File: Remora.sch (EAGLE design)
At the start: 81 parts, among them IC1 MCP23017, J2 GROVE-I2C, P1 PADSMALL, T1 2N3904, T2 BSS138

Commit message: Mise à jour du PCB et ajout d'images
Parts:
- RELAIS: value G3MC-202P -> G3MC-202P-5V
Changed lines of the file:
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@@
 <grid distance="0.1" unitdist="inch" unit="inch" style="lines" multiple="1" display="no" altdistance="0.01" altunitdist="inch" altunit="inch"/>
 <layers>
-<layer number="1" name="Top" color="4" fill="1" visible="no" active="no"/>
-<layer number="2" name="Route2" color="1" fill="3" visible="no" active="no"/>
-<layer number="3" name="Route3" color="4" fill="3" visible="no" active="no"/>
-<layer number="4" name="Route4" color="1" fill="4" visible="no" active="no"/>
-<layer number="5" name="Route5" color="4" fill="4" visible="no" active="no"/>
-<layer number="6" name="Route6" color="1" fill="8" visible="no" active="no"/>
-<layer number="7" name="Route7" color="4" fill="8" visible="no" active="no"/>
-<layer number="8" name="Route8" color="1" fill="2" visible="no" active="no"/>
-<layer number="9" name="Route9" color="4" fill="2" visible="no" active="no"/>
-<layer number="10" name="Route10" color="1" fill="7" visible="no" active="no"/>
-<layer number="11" name="Route11" color="4" fill="7" visible="no" active="no"/>
-<layer number="12" name="Route12" color="1" fill="5" visible="no" active="no"/>
-<layer number="13" name="Route13" color="4" fill="5" visible="no" active="no"/>
-<layer number="14" name="Route14" color="1" fill="6" visible="no" active="no"/>
-<layer number="15" name="Route15" color="4" fill="6" visible="no" active="no"/>
-<layer number="16" name="Bottom" color="1" fill="1" visible="no" active="no"/>
-<layer number="17" name="Pads" color="2" fill="1" visible="no" active="no"/>
-<layer number="18" name="Vias" color="2" fill="1" visible="no" active="no"/>
-<layer number="19" name="Unrouted" color="13" fill="1" visible="no" active="no"/>
-<layer number="20" name="Dimension" color="15" fill="1" visible="no" active="no"/>
-<layer number="21" name="tPlace" color="7" fill="1" visible="no" active="no"/>
-<layer number="22" name="bPlace" color="3" fill="1" visible="no" active="no"/>
-<layer number="23" name="tOrigins" color="15" fill="1" visible="no" active="no"/>
-<layer number="24" name="bOrigins" color="3" fill="1" visible="no" active="no"/>
-<layer number="25" name="tNames" color="7" fill="1" visible="no" active="no"/>
-<layer number="26" name="bNames" color="3" fill="1" visible="no" active="no"/>
-<layer number="27" name="tValues" color="7" fill="1" visible="no" active="no"/>
-<layer number="28" name="bValues" color="3" fill="1" visible="no" active="no"/>
+<layer number="1" name="Top" color="4" fill="1" visible="yes" active="no"/>
+<layer number="2" name="Route2" color="1" fill="3" visible="yes" active="no"/>
+<layer number="3" name="Route3" color="4" fill="3" visible="yes" active="no"/>
+<layer number="4" name="Route4" color="1" fill="4" visible="yes" active="no"/>
+<layer number="5" name="Route5" color="4" fill="4" visible="yes" active="no"/>
+<layer number="6" name="Route6" color="1" fill="8" visible="yes" active="no"/>
+<layer number="7" name="Route7" color="4" fill="8" visible="yes" active="no"/>
+<layer number="8" name="Route8" color="1" fill="2" visible="yes" active="no"/>
+<layer number="9" name="Route9" color="4" fill="2" visible="yes" active="no"/>
+<layer number="10" name="Route10" color="1" fill="7" visible="yes" active="no"/>
+<layer number="11" name="Route11" color="4" fill="7" visible="yes" active="no"/>
+<layer number="12" name="Route12" color="1" fill="5" visible="yes" active="no"/>
+<layer number="13" name="Route13" color="4" fill="5" visible="yes" active="no"/>
+<layer number="14" name="Route14" color="1" fill="6" visible="yes" active="no"/>
+<layer number="15" name="Route15" color="4" fill="6" visible="yes" active="no"/>
+<layer number="16" name="Bottom" color="1" fill="1" visible="yes" active="no"/>
+<layer number="17" name="Pads" color="2" fill="1" visible="yes" active="no"/>
+<layer number="18" name="Vias" color="2" fill="1" visible="yes" active="no"/>
+<layer number="19" name="Unrouted" color="13" fill="1" visible="yes" active="no"/>
+<layer number="20" name="Dimension" color="15" fill="1" visible="yes" active="no"/>
+<layer number="21" name="tPlace" color="7" fill="1" visible="yes" active="no"/>
+<layer number="22" name="bPlace" color="3" fill="1" visible="yes" active="no"/>
+<layer number="23" name="tOrigins" color="15" fill="1" visible="yes" active="no"/>
+<layer number="24" name="bOrigins" color="3" fill="1" visible="yes" active="no"/>
+<layer number="25" name="tNames" color="7" fill="1" visible="yes" active="no"/>
+<layer number="26" name="bNames" color="3" fill="1" visible="yes" active="no"/>
+<layer number="27" name="tValues" color="7" fill="1" visible="yes" active="no"/>
+<layer number="28" name="bValues" color="3" fill="1" visible="yes" active="no"/>
 <layer number="29" name="tStop" color="7" fill="3" visible="no" active="no"/>
 <layer number="30" name="bStop" color="7" fill="6" visible="no" active="no"/>
@@
 <layer number="35" name="tGlue" color="7" fill="4" visible="no" active="no"/>
 <layer number="36" name="bGlue" color="7" fill="5" visible="no" active="no"/>
-<layer number="37" name="tTest" color="7" fill="1" visible="no" active="no"/>
-<layer number="38" name="bTest" color="7" fill="1" visible="no" active="no"/>
+<layer number="37" name="tTest" color="7" fill="1" visible="yes" active="no"/>
+<layer number="38" name="bTest" color="7" fill="1" visible="yes" active="no"/>
 <layer number="39" name="tKeepout" color="4" fill="11" visible="no" active="no"/>
 <layer number="40" name="bKeepout" color="1" fill="11" visible="no" active="no"/>
@@
 <layer number="44" name="Drills" color="7" fill="1" visible="no" active="no"/>
 <layer number="45" name="Holes" color="7" fill="1" visible="no" active="no"/>
-<layer number="46" name="Milling" color="3" fill="1" visible="no" active="no"/>
-<layer number="47" name="Measures" color="7" fill="1" visible="no" active="no"/>
-<layer number="48" name="Document" color="7" fill="1" visible="no" active="no"/>
-<layer number="49" name="Reference" color="7" fill="1" visible="no" active="no"/>
-<layer number="50" name="dxf" color="7" fill="1" visible="no" active="no"/>
-<layer number="51" name="tDocu" color="7" fill="1" visible="no" active="no"/>
-<layer number="52" name="bDocu" color="3" fill="1" visible="no" active="no"/>
-<layer number="53" name="tGND_GNDA" color="7" fill="9" visible="no" active="no"/>
-<layer number="54" name="bGND_GNDA" color="1" fill="9" visible="no" active="no"/>
-<layer number="56" name="wert" color="7" fill="1" visible="no" active="no"/>
-<layer number="57" name="tCAD" color="7" fill="1" visible="no" active="no"/>
-<layer number="59" name="tCarbon" color="7" fill="1" visible="no" active="no"/>
-<layer number="60" name="bCarbon" color="7" fill="1" visible="no" active="no"/>
+<layer number="46" name="Milling" color="3" fill="1" visible="yes" active="no"/>
+<layer number="47" name="Measures" color="7" fill="1" visible="yes" active="no"/>
+<layer number="48" name="Document" color="7" fill="1" visible="yes" active="no"/>
+<layer number="49" name="Reference" color="7" fill="1" visible="yes" active="no"/>
+<layer number="50" name="dxf" color="7" fill="1" visible="yes" active="no"/>
+<layer number="51" name="tDocu" color="7" fill="1" visible="yes" active="no"/>
+<layer number="52" name="bDocu" color="3" fill="1" visible="yes" active="no"/>
+<layer number="53" name="tGND_GNDA" color="7" fill="9" visible="yes" active="no"/>
+<layer number="54" name="bGND_GNDA" color="1" fill="9" visible="yes" active="no"/>
+<layer number="56" name="wert" color="7" fill="1" visible="yes" active="no"/>
+<layer number="57" name="tCAD" color="7" fill="1" visible="yes" active="no"/>
+<layer number="59" name="tCarbon" color="7" fill="1" visible="yes" active="no"/>
+<layer number="60" name="bCarbon" color="7" fill="1" visible="yes" active="no"/>
 <layer number="90" name="Modules" color="5" fill="1" visible="yes" active="yes"/>
 <layer number="91" name="Nets" color="2" fill="1" visible="yes" active="yes"/>
@@
 <part name="JP1" library="SparkFun-Connectors" deviceset="M02" device="PTH"/>
 <part name="230V" library="con-ptr500" deviceset="AK500/3" device=""/>
-<part name="RELAIS" library="sip-4" deviceset="G3MC-202P" device=""/>
+<part name="RELAIS" library="sip-4" deviceset="G3MC-202P" device="" value="G3MC-202P-5V"/>
 </parts>
 <sheets>

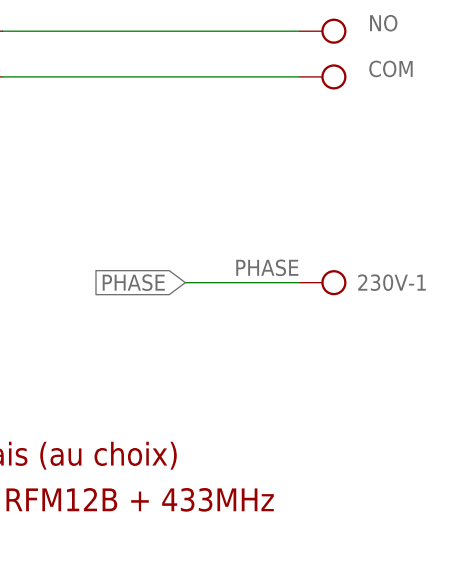
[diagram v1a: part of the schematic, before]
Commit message: Correction d'anomalie de la route de la phase
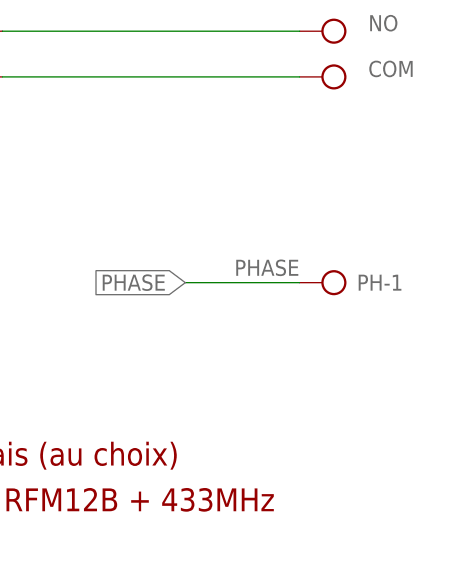
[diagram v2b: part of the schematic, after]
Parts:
- renumbered 230V to PH
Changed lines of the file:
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@@
 <grid distance="0.1" unitdist="inch" unit="inch" style="lines" multiple="1" display="no" altdistance="0.01" altunitdist="inch" altunit="inch"/>
 <layers>
-<layer number="1" name="Top" color="4" fill="1" visible="yes" active="no"/>
-<layer number="2" name="Route2" color="1" fill="3" visible="yes" active="no"/>
-<layer number="3" name="Route3" color="4" fill="3" visible="yes" active="no"/>
-<layer number="4" name="Route4" color="1" fill="4" visible="yes" active="no"/>
-<layer number="5" name="Route5" color="4" fill="4" visible="yes" active="no"/>
-<layer number="6" name="Route6" color="1" fill="8" visible="yes" active="no"/>
-<layer number="7" name="Route7" color="4" fill="8" visible="yes" active="no"/>
-<layer number="8" name="Route8" color="1" fill="2" visible="yes" active="no"/>
-<layer number="9" name="Route9" color="4" fill="2" visible="yes" active="no"/>
-<layer number="10" name="Route10" color="1" fill="7" visible="yes" active="no"/>
-<layer number="11" name="Route11" color="4" fill="7" visible="yes" active="no"/>
-<layer number="12" name="Route12" color="1" fill="5" visible="yes" active="no"/>
-<layer number="13" name="Route13" color="4" fill="5" visible="yes" active="no"/>
-<layer number="14" name="Route14" color="1" fill="6" visible="yes" active="no"/>
-<layer number="15" name="Route15" color="4" fill="6" visible="yes" active="no"/>
-<layer number="16" name="Bottom" color="1" fill="1" visible="yes" active="no"/>
-<layer number="17" name="Pads" color="2" fill="1" visible="yes" active="no"/>
-<layer number="18" name="Vias" color="2" fill="1" visible="yes" active="no"/>
-<layer number="19" name="Unrouted" color="13" fill="1" visible="yes" active="no"/>
-<layer number="20" name="Dimension" color="15" fill="1" visible="yes" active="no"/>
-<layer number="21" name="tPlace" color="7" fill="1" visible="yes" active="no"/>
-<layer number="22" name="bPlace" color="3" fill="1" visible="yes" active="no"/>
-<layer number="23" name="tOrigins" color="15" fill="1" visible="yes" active="no"/>
-<layer number="24" name="bOrigins" color="3" fill="1" visible="yes" active="no"/>
-<layer number="25" name="tNames" color="7" fill="1" visible="yes" active="no"/>
-<layer number="26" name="bNames" color="3" fill="1" visible="yes" active="no"/>
-<layer number="27" name="tValues" color="7" fill="1" visible="yes" active="no"/>
-<layer number="28" name="bValues" color="3" fill="1" visible="yes" active="no"/>
+<layer number="1" name="Top" color="4" fill="1" visible="no" active="no"/>
+<layer number="2" name="Route2" color="1" fill="3" visible="no" active="no"/>
+<layer number="3" name="Route3" color="4" fill="3" visible="no" active="no"/>
+<layer number="4" name="Route4" color="1" fill="4" visible="no" active="no"/>
+<layer number="5" name="Route5" color="4" fill="4" visible="no" active="no"/>
+<layer number="6" name="Route6" color="1" fill="8" visible="no" active="no"/>
+<layer number="7" name="Route7" color="4" fill="8" visible="no" active="no"/>
+<layer number="8" name="Route8" color="1" fill="2" visible="no" active="no"/>
+<layer number="9" name="Route9" color="4" fill="2" visible="no" active="no"/>
+<layer number="10" name="Route10" color="1" fill="7" visible="no" active="no"/>
+<layer number="11" name="Route11" color="4" fill="7" visible="no" active="no"/>
+<layer number="12" name="Route12" color="1" fill="5" visible="no" active="no"/>
+<layer number="13" name="Route13" color="4" fill="5" visible="no" active="no"/>
+<layer number="14" name="Route14" color="1" fill="6" visible="no" active="no"/>
+<layer number="15" name="Route15" color="4" fill="6" visible="no" active="no"/>
+<layer number="16" name="Bottom" color="1" fill="1" visible="no" active="no"/>
+<layer number="17" name="Pads" color="2" fill="1" visible="no" active="no"/>
+<layer number="18" name="Vias" color="2" fill="1" visible="no" active="no"/>
+<layer number="19" name="Unrouted" color="13" fill="1" visible="no" active="no"/>
+<layer number="20" name="Dimension" color="15" fill="1" visible="no" active="no"/>
+<layer number="21" name="tPlace" color="7" fill="1" visible="no" active="no"/>
+<layer number="22" name="bPlace" color="3" fill="1" visible="no" active="no"/>
+<layer number="23" name="tOrigins" color="15" fill="1" visible="no" active="no"/>
+<layer number="24" name="bOrigins" color="3" fill="1" visible="no" active="no"/>
+<layer number="25" name="tNames" color="7" fill="1" visible="no" active="no"/>
+<layer number="26" name="bNames" color="3" fill="1" visible="no" active="no"/>
+<layer number="27" name="tValues" color="7" fill="1" visible="no" active="no"/>
+<layer number="28" name="bValues" color="3" fill="1" visible="no" active="no"/>
 <layer number="29" name="tStop" color="7" fill="3" visible="no" active="no"/>
 <layer number="30" name="bStop" color="7" fill="6" visible="no" active="no"/>
@@
 <layer number="35" name="tGlue" color="7" fill="4" visible="no" active="no"/>
 <layer number="36" name="bGlue" color="7" fill="5" visible="no" active="no"/>
-<layer number="37" name="tTest" color="7" fill="1" visible="yes" active="no"/>
-<layer number="38" name="bTest" color="7" fill="1" visible="yes" active="no"/>
+<layer number="37" name="tTest" color="7" fill="1" visible="no" active="no"/>
+<layer number="38" name="bTest" color="7" fill="1" visible="no" active="no"/>
 <layer number="39" name="tKeepout" color="4" fill="11" visible="no" active="no"/>
 <layer number="40" name="bKeepout" color="1" fill="11" visible="no" active="no"/>
@@
 <layer number="44" name="Drills" color="7" fill="1" visible="no" active="no"/>
 <layer number="45" name="Holes" color="7" fill="1" visible="no" active="no"/>
-<layer number="46" name="Milling" color="3" fill="1" visible="yes" active="no"/>
-<layer number="47" name="Measures" color="7" fill="1" visible="yes" active="no"/>
-<layer number="48" name="Document" color="7" fill="1" visible="yes" active="no"/>
-<layer number="49" name="Reference" color="7" fill="1" visible="yes" active="no"/>
-<layer number="50" name="dxf" color="7" fill="1" visible="yes" active="no"/>
-<layer number="51" name="tDocu" color="7" fill="1" visible="yes" active="no"/>
-<layer number="52" name="bDocu" color="3" fill="1" visible="yes" active="no"/>
-<layer number="53" name="tGND_GNDA" color="7" fill="9" visible="yes" active="no"/>
-<layer number="54" name="bGND_GNDA" color="1" fill="9" visible="yes" active="no"/>
-<layer number="56" name="wert" color="7" fill="1" visible="yes" active="no"/>
-<layer number="57" name="tCAD" color="7" fill="1" visible="yes" active="no"/>
-<layer number="59" name="tCarbon" color="7" fill="1" visible="yes" active="no"/>
-<layer number="60" name="bCarbon" color="7" fill="1" visible="yes" active="no"/>
+<layer number="46" name="Milling" color="3" fill="1" visible="no" active="no"/>
+<layer number="47" name="Measures" color="7" fill="1" visible="no" active="no"/>
+<layer number="48" name="Document" color="7" fill="1" visible="no" active="no"/>
+<layer number="49" name="Reference" color="7" fill="1" visible="no" active="no"/>
+<layer number="50" name="dxf" color="7" fill="1" visible="no" active="no"/>
+<layer number="51" name="tDocu" color="7" fill="1" visible="no" active="no"/>
+<layer number="52" name="bDocu" color="3" fill="1" visible="no" active="no"/>
+<layer number="53" name="tGND_GNDA" color="7" fill="9" visible="no" active="no"/>
+<layer number="54" name="bGND_GNDA" color="1" fill="9" visible="no" active="no"/>
+<layer number="56" name="wert" color="7" fill="1" visible="no" active="no"/>
+<layer number="57" name="tCAD" color="7" fill="1" visible="no" active="no"/>
+<layer number="59" name="tCarbon" color="7" fill="1" visible="no" active="no"/>
+<layer number="60" name="bCarbon" color="7" fill="1" visible="no" active="no"/>
 <layer number="90" name="Modules" color="5" fill="1" visible="yes" active="yes"/>
 <layer number="91" name="Nets" color="2" fill="1" visible="yes" active="yes"/>
@@
 <part name="X1" library="con-ptr500" deviceset="AK500/3" device=""/>
 <part name="JP1" library="SparkFun-Connectors" deviceset="M02" device="PTH"/>
-<part name="230V" library="con-ptr500" deviceset="AK500/3" device=""/>
+<part name="PH" library="con-ptr500" deviceset="AK500/3" device=""/>
 <part name="RELAIS" library="sip-4" deviceset="G3MC-202P" device="" value="G3MC-202P-5V"/>
 </parts>
@@
 <instance part="X1" gate="-3" x="-152.4" y="45.72"/>
 <instance part="JP1" gate="G$1" x="-156.21" y="67.31"/>
-<instance part="230V" gate="-1" x="48.26" y="-86.36" smashed="yes" rot="R180">
+<instance part="PH" gate="-1" x="48.26" y="-86.36" smashed="yes" rot="R180">
 <attribute name="NAME" x="49.53" y="-87.249" size="1.778" layer="95"/>
 </instance>
-<instance part="230V" gate="-2" x="48.26" y="-58.42" smashed="yes" rot="R180"/>
-<instance part="230V" gate="-3" x="48.26" y="-63.5" smashed="yes" rot="R180">
+<instance part="PH" gate="-2" x="48.26" y="-58.42" smashed="yes" rot="R180"/>
+<instance part="PH" gate="-3" x="48.26" y="-63.5" smashed="yes" rot="R180">
 <attribute name="VALUE" x="52.07" y="-59.817" size="1.778" layer="96" rot="R180"/>
 </instance>
@@
 <wire x1="43.18" y1="-86.36" x2="30.48" y2="-86.36" width="0.1524" layer="91"/>
 <label x="43.18" y="-83.82" size="1.778" layer="95" rot="R180"/>
-<pinref part="230V" gate="-1" pin="KL"/>
+<pinref part="PH" gate="-1" pin="KL"/>
 </segment>
 <segment>
@@
 <segment>
 <pinref part="RELAIS" gate="G$1" pin="1"/>
-<pinref part="230V" gate="-2" pin="KL"/>
+<pinref part="PH" gate="-2" pin="KL"/>
 <wire x1="10.16" y1="-58.42" x2="43.18" y2="-58.42" width="0.1524" layer="91"/>
 <label x="50.8" y="-58.42" size="1.778" layer="95"/>
@@
 <segment>
 <pinref part="RELAIS" gate="G$1" pin="2"/>
-<pinref part="230V" gate="-3" pin="KL"/>
+<pinref part="PH" gate="-3" pin="KL"/>
 <wire x1="10.16" y1="-63.5" x2="43.18" y2="-63.5" width="0.1524" layer="91"/>
 <label x="50.8" y="-63.5" size="1.778" layer="95"/>
